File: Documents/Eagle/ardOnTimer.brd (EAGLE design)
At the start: 53.3 x 59.7 mm, 15 parts

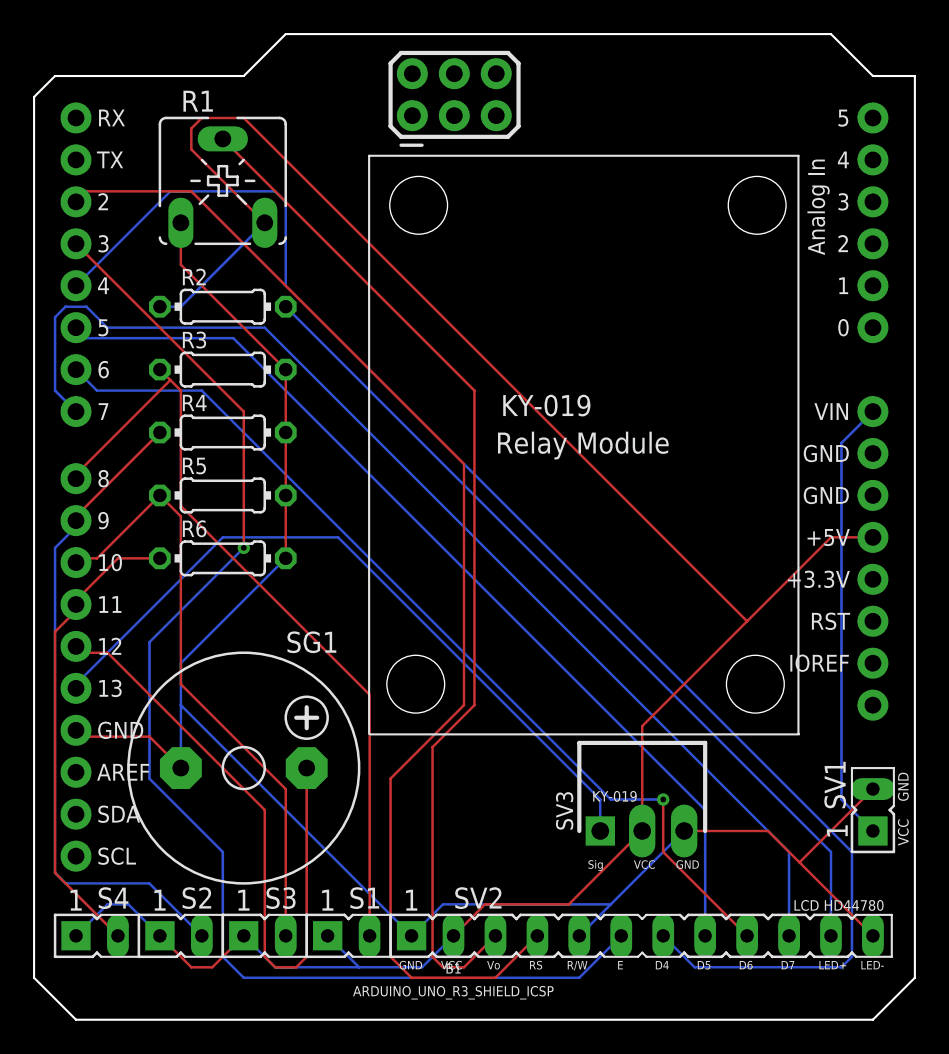
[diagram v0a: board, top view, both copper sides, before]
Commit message: Switched DI12<->DI13
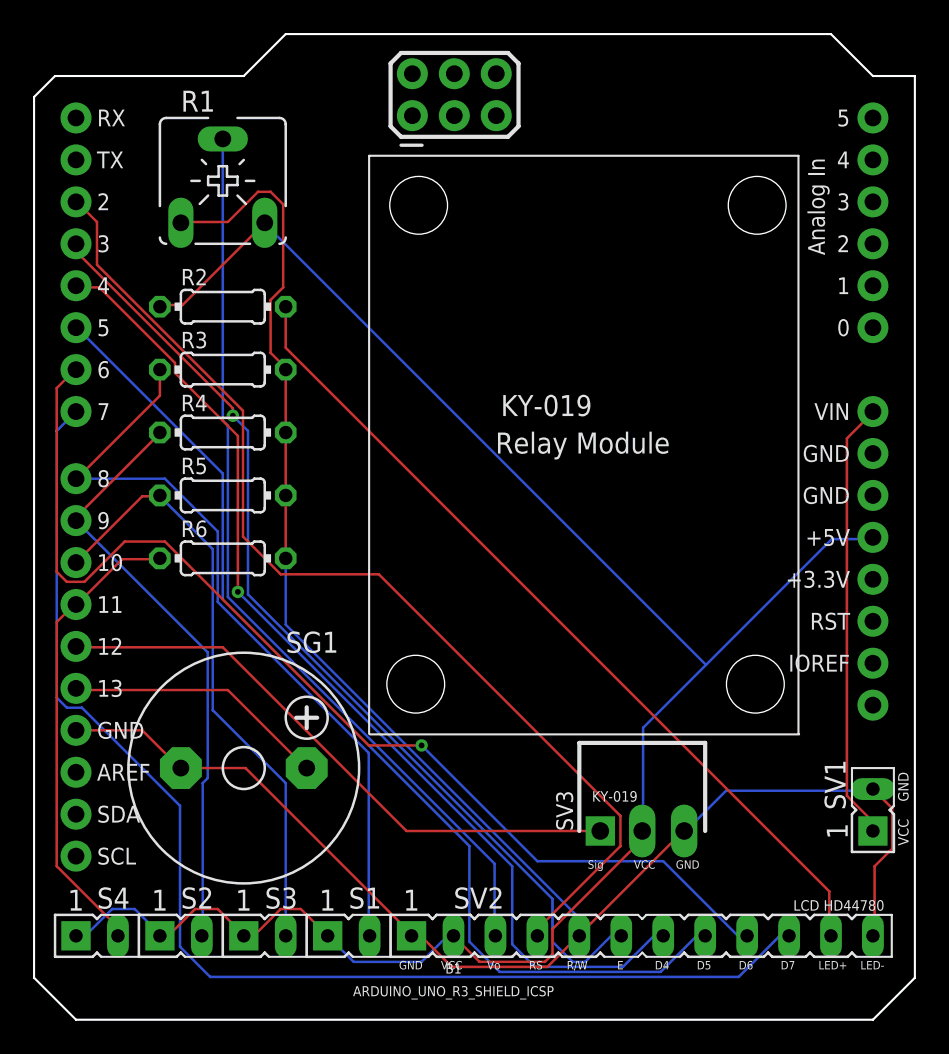
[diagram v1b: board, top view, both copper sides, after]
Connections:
- removed net N$19: B1.D13, SV3.SIG
- new net N$17: B1.D12, SV3.SIG
- net N$2: now also B1.D13; no longer B1.D12
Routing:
- net N$19: track 44.2 -> 0.00 mm
- net N$17: track 0.00 -> 36.4 mm
- net N$7: track 87.7 -> 62.1 mm, vias 0 -> 1
- net N$2: track 39.1 -> 16.0 mm
- net N$1: track 107.7 -> 128.3 mm
- net N$6: track 77.3 -> 59.5 mm
- net N$12: track 132.0 -> 116.3 mm
- net N$5: track 72.8 -> 63.7 mm
- net N$9: track 56.7 -> 65.7 mm
- net N$3: track 61.8 -> 55.1 mm
- net N$10: track 69.7 -> 75.2 mm
- net N$8: track 57.8 -> 63.0 mm
- net N$14: track 39.8 -> 36.1 mm
- net N$13: track 47.9 -> 46.9 mm

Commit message: Forgot resistor in schematics. Updated readme.
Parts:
- added R7: 100R, rcl:0204/7
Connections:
- new net N$18: R7.2, SG1.-
- net N$1: now also R7.1; no longer SG1.-
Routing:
- net N$18: track 0.00 -> 21.9 mm
- net N$9: track 65.7 -> 80.5 mm, vias 1 -> 0
- net N$7: track 62.1 -> 75.5 mm, vias 1 -> 0
- net N$14: track 36.1 -> 43.9 mm
- net N$6: track 59.5 -> 65.8 mm, vias 1 -> 0
- net N$4: track 51.8 -> 57.5 mm
- net N$10: track 75.2 -> 69.8 mm
- net N$8: track 63.0 -> 68.4 mm
- net N$5: track 63.7 -> 60.3 mm
- net N$1: track 128.3 -> 125.3 mm
- net N$16: track 28.4 -> 26.7 mm
- net N$13: track 46.9 -> 47.9 mm
- net N$11: track 26.7 -> 27.6 mm
